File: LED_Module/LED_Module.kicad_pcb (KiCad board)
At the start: 2 copper layers, 25 x 25 mm, 13 parts, among them P1 CONN_01X01, P2 CONN_01X01, P3 CONN_01X01, P4 CONN_01X01, P5 CONN_01X01, U1 AL8805WS

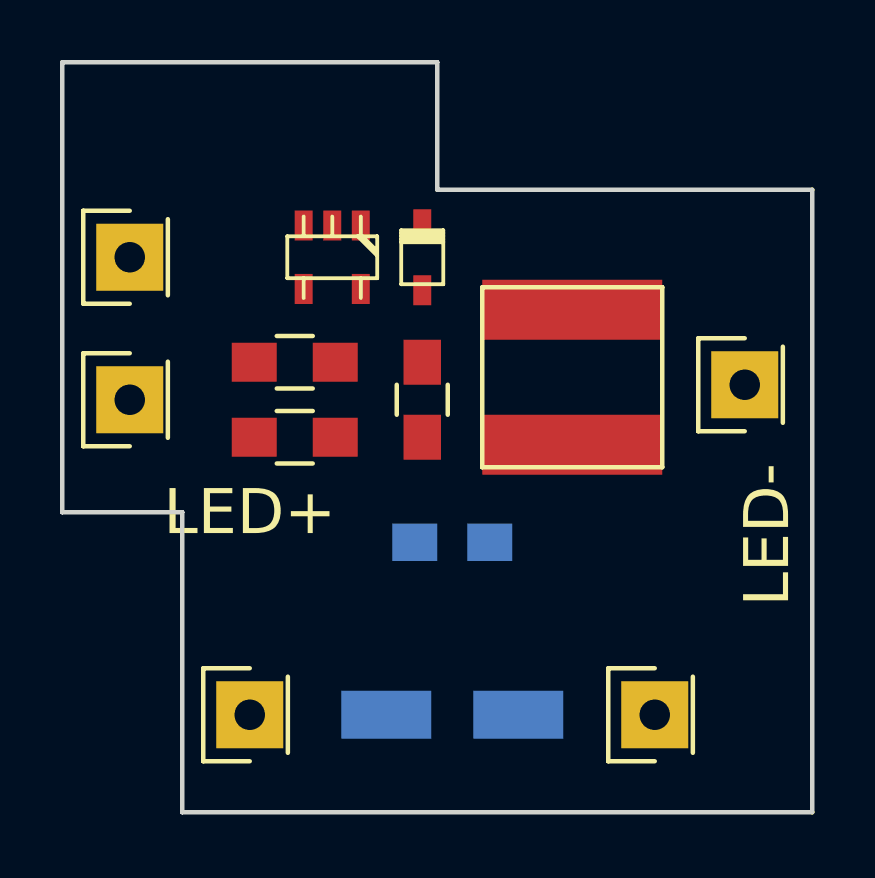
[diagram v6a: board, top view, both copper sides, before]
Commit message: LED Module Routing
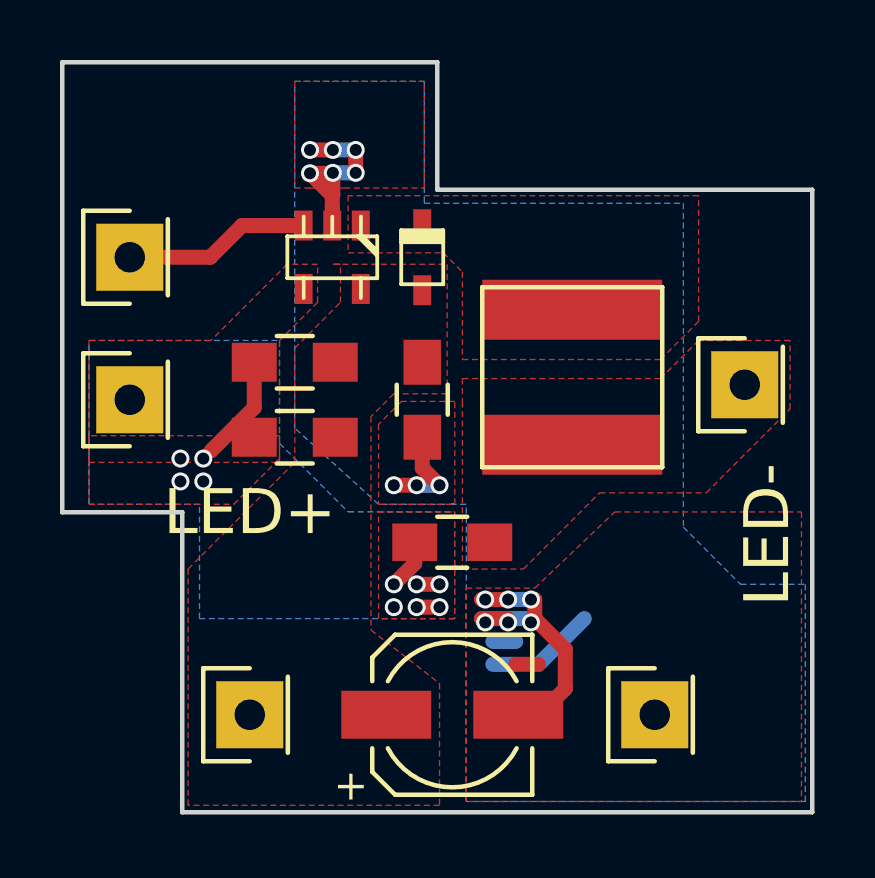
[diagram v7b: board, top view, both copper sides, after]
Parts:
- C1, C2: moved to F.Cu
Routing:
- net GND: track 0.00 -> 20.6 mm, vias 0 -> 15
- net /LED1+: track 0.00 -> 6.77 mm, vias 0 -> 10
- net /CTRL_PWM: track 0.00 -> 6.24 mm
- net (no net): track 0.00 -> 4.44 mm
- added copper zone on B.Cu, net /LED1+
- added copper zone on F.Cu, net /LED1+
- added copper zone on F.Cu, net /LED1-
- added copper zone on F.Cu, net /V_BAT
- added copper zone on B.Cu, net GND
- added copper zone on F.Cu, net GND
- added copper zone on F.Cu, net Net-(D1-Pad2)

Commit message: LED-MODULE : resize pad
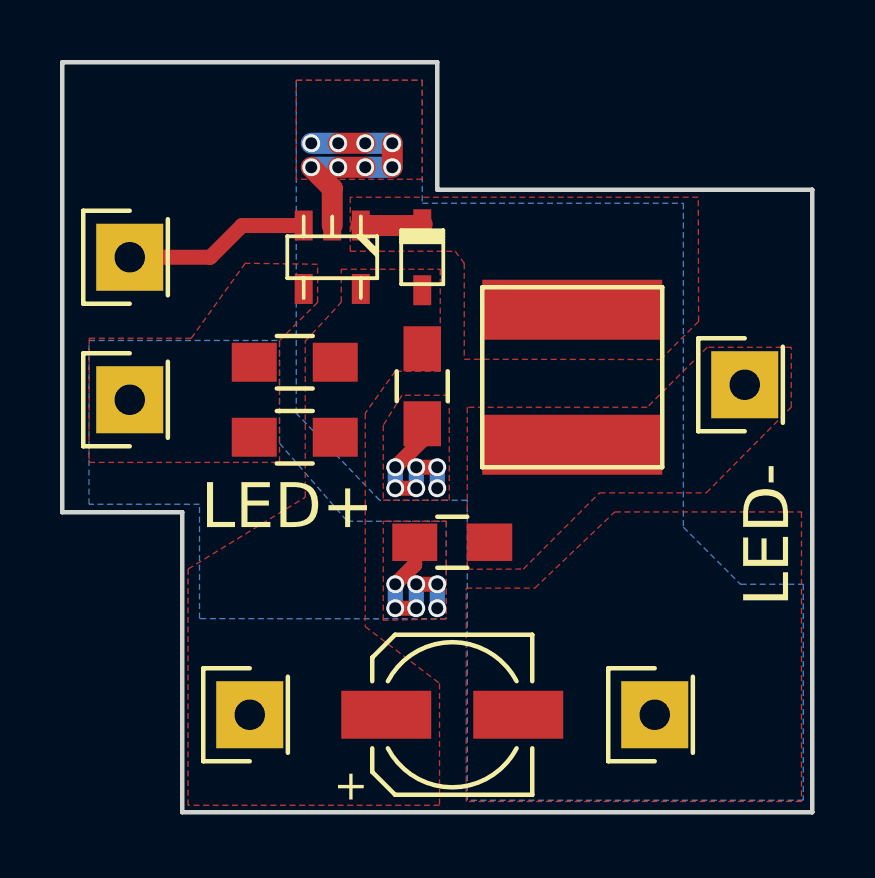
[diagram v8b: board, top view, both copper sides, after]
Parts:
- moved C3 0.45 mm to (99.5, 98.3)
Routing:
- net GND: track 20.6 -> 14.5 mm, vias 15 -> 14
- net (no net): track 4.44 -> 0.00 mm
- net Net-(D1-Pad2): track 0.00 -> 2.07 mm
- net /LED1+: track 6.77 -> 5.47 mm, vias 10 -> 6
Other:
- net class Default: trace_width 0.5 -> 0.7
